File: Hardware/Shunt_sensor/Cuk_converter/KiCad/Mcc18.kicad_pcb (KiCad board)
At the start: 2 copper layers, 199.1 x 118.4 mm, 62 parts, among them Q1 IRFP4321PbF, U1 INA240, U2 DRIVER_(INEP), U3 LM7812_TO220, U4 Signals_MCC, U5 ZCS, U6 INA211

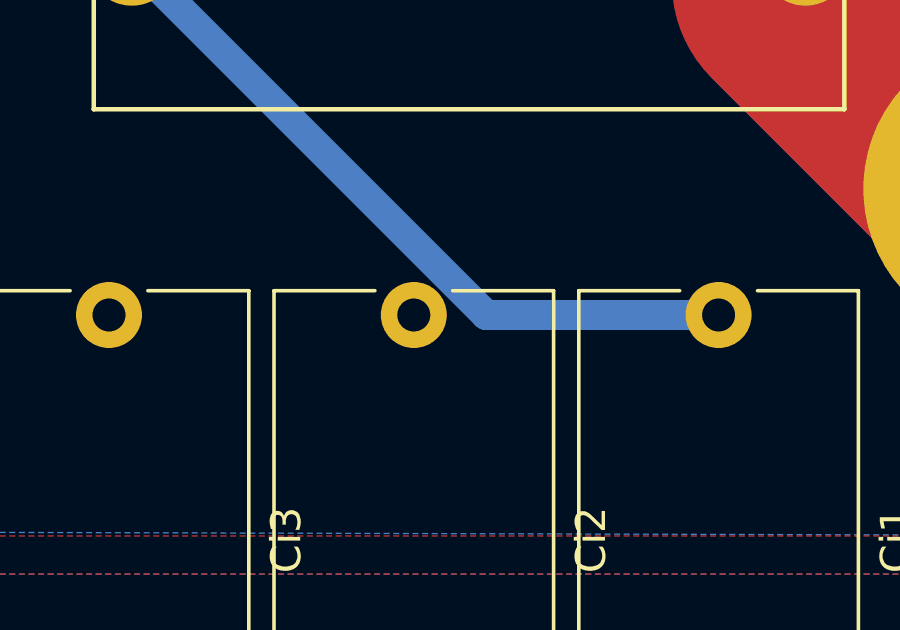
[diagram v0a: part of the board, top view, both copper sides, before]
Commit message: crated new fill zones and minimized holes sizes
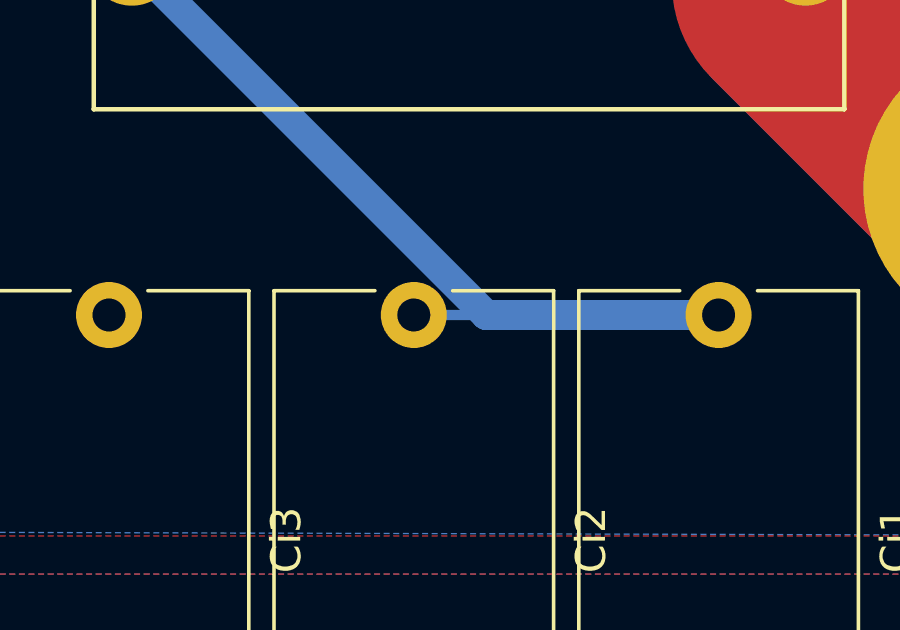
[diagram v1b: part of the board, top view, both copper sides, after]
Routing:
- net /-Vp: track 146.4 -> 148.8 mm
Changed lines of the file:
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@@
     (thickness 1.6)
     (drawings 13)
-    (tracks 671)
+    (tracks 672)
     (zones 0)
     (modules 62)
@@
   (segment (start 126.03734 54.1986) (end 127.40124 55.5625) (width 0.508) (layer B.Cu) (net 46))
   (segment (start 127.40124 55.5625) (end 129.13108 55.5625) (width 0.508) (layer B.Cu) (net 46))
+  (segment (start 220.218 59.182) (end 222.631 59.182) (width 0.3429) (layer B.Cu) (net 46))
   (segment (start 92.075 140.716) (end 91.948 140.843) (width 0.508) (layer B.Cu) (net 50) (status 30))
   (segment (start 105.81 108.966) (end 105.41 108.966) (width 0.635) (layer F.Cu) (net 51) (status 40000))
